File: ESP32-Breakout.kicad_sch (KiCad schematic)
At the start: 3 parts, among them U1 ESP32-S2-DevKitC-1

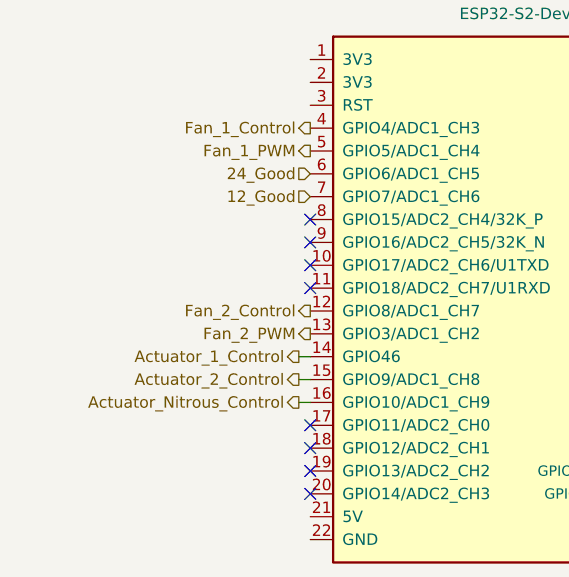
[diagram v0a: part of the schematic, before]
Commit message: Placed the general sets of components.
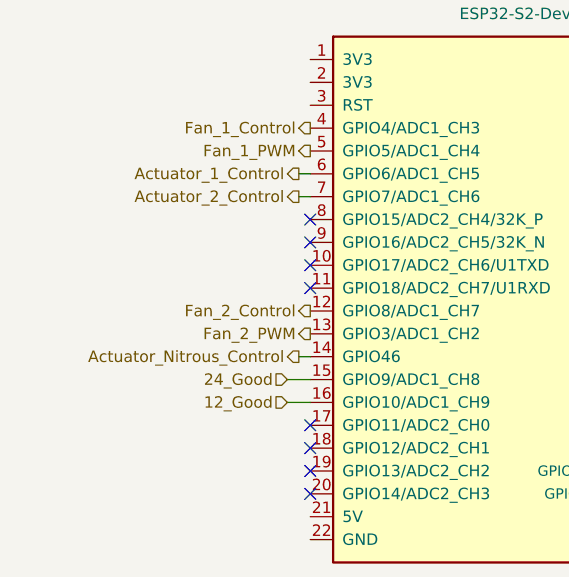
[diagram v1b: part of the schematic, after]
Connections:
- net 12_Good: now also U1.16 (GPIO10/ADC1_CH9); no longer U1.7 (GPIO7/ADC1_CH6)
- net 24_Good: now also U1.15 (GPIO9/ADC1_CH8); no longer U1.6 (GPIO6/ADC1_CH5)
- net Actuator_1_Control: now also U1.6 (GPIO6/ADC1_CH5); no longer U1.14 (GPIO46)
- net Actuator_2_Control: now also U1.7 (GPIO7/ADC1_CH6); no longer U1.15 (GPIO9/ADC1_CH8)
- net Actuator_Nitrous_Control: now also U1.14 (GPIO46); no longer U1.16 (GPIO10/ADC1_CH9)
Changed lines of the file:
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@@
 	(wire
 		(pts
-			(xy 80.01 77.47) (xy 81.28 77.47)
-		)
-		(stroke
-			(width 0)
-			(type default)
-		)
-	)
-	(wire
-		(pts
-			(xy 80.01 74.93) (xy 81.28 74.93)
+			(xy 78.74 77.47) (xy 81.28 77.47)
+		)
+		(stroke
+			(width 0)
+			(type default)
+		)
+	)
+	(wire
+		(pts
+			(xy 78.74 74.93) (xy 81.28 74.93)
 		)
 		(stroke
@@
 		(pts
 			(xy 80.01 72.39) (xy 81.28 72.39)
+		)
+		(stroke
+			(width 0)
+			(type default)
+		)
+	)
+	(wire
+		(pts
+			(xy 80.01 52.07) (xy 81.28 52.07)
+		)
+		(stroke
+			(width 0)
+			(type default)
+		)
+	)
+	(wire
+		(pts
+			(xy 80.01 54.61) (xy 81.28 54.61)
 		)
 		(stroke
@@
 		)
 	)
+	(hierarchical_label "Actuator_Nitrous_Control"
+		(shape output)
+		(at 80.01 72.39 180)
+		(effects
+			(font
+				(size 1.27 1.27)
+			)
+			(justify right)
+		)
+	)
+	(hierarchical_label "Actuator_2_Control"
+		(shape output)
+		(at 80.01 54.61 180)
+		(effects
+			(font
+				(size 1.27 1.27)
+			)
+			(justify right)
+		)
+	)
 	(hierarchical_label "DRDY2"
 		(shape input)
@@
 		)
 	)
-	(hierarchical_label "Actuator_Nitrous_Control"
-		(shape output)
-		(at 80.01 77.47 180)
+	(hierarchical_label "24_Good"
+		(shape input)
+		(at 78.74 74.93 180)
 		(effects
 			(font
@@
 		)
 	)
-	(hierarchical_label "Actuator_2_Control"
-		(shape output)
-		(at 80.01 74.93 180)
+	(hierarchical_label "Actuator_1_Control"
+		(shape output)
+		(at 80.01 52.07 180)
+		(effects
+			(font
+				(size 1.27 1.27)
+			)
+			(justify right)
+		)
+	)
+	(hierarchical_label "12_Good"
+		(shape input)
+		(at 78.74 77.47 180)
 		(effects
 			(font
@@
 		)
 	)
-	(hierarchical_label "24_Good"
-		(shape input)
-		(at 81.28 52.07 180)
-		(effects
-			(font
-				(size 1.27 1.27)
-			)
-			(justify right)
-		)
-	)
-	(hierarchical_label "12_Good"
-		(shape input)
-		(at 81.28 54.61 180)
-		(effects
-			(font
-				(size 1.27 1.27)
-			)
-			(justify right)
-		)
-	)
 	(hierarchical_label "DRDY1"
 		(shape input)
@@
 		(effects
 			(font
-				(size 1.27 1.27)
-			)
-			(justify right)
-		)
-	)
-	(hierarchical_label "Actuator_1_Control"
-		(shape output)
-		(at 80.01 72.39 180)
-		(effects
-			(font

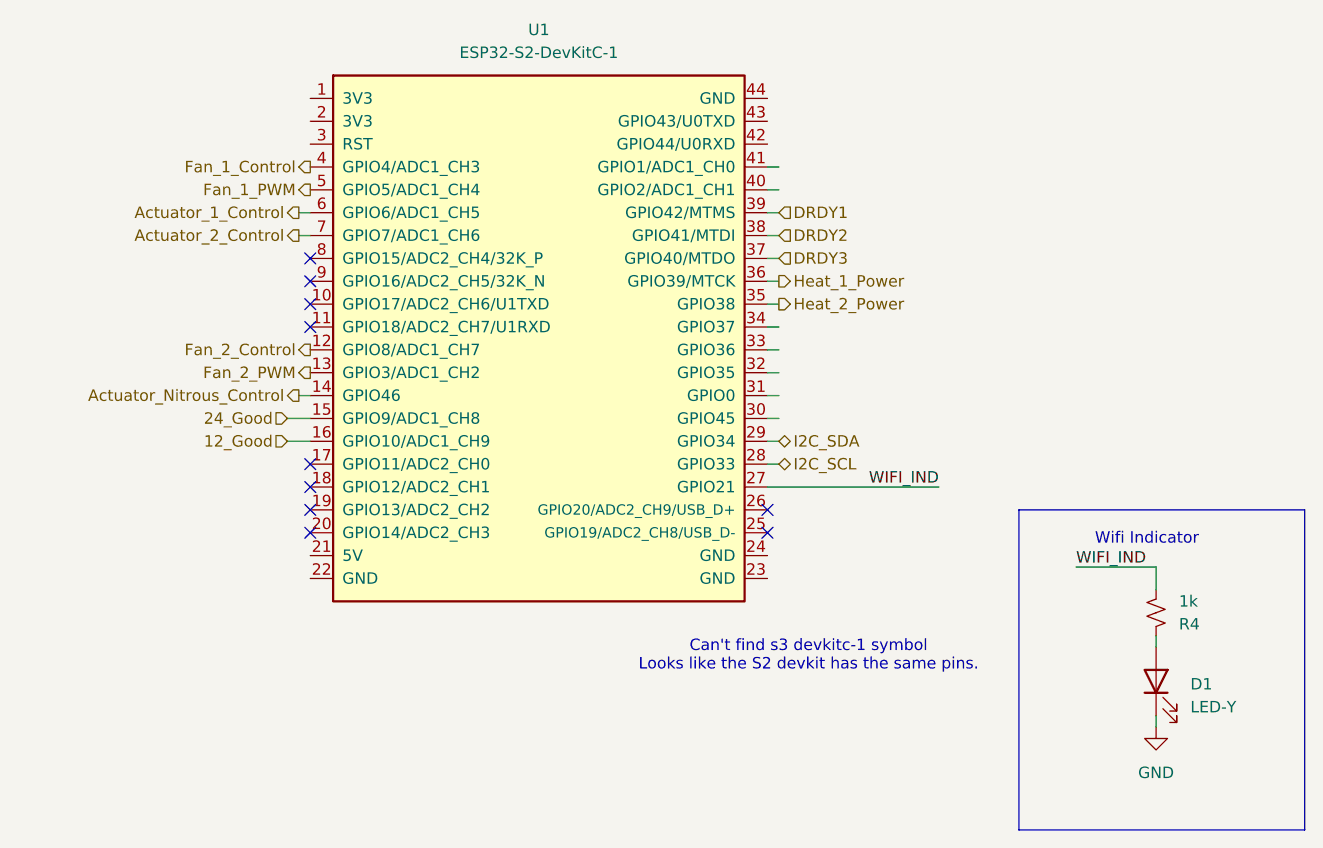
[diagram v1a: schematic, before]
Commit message: General board shape, mounting holes, grounding plates.
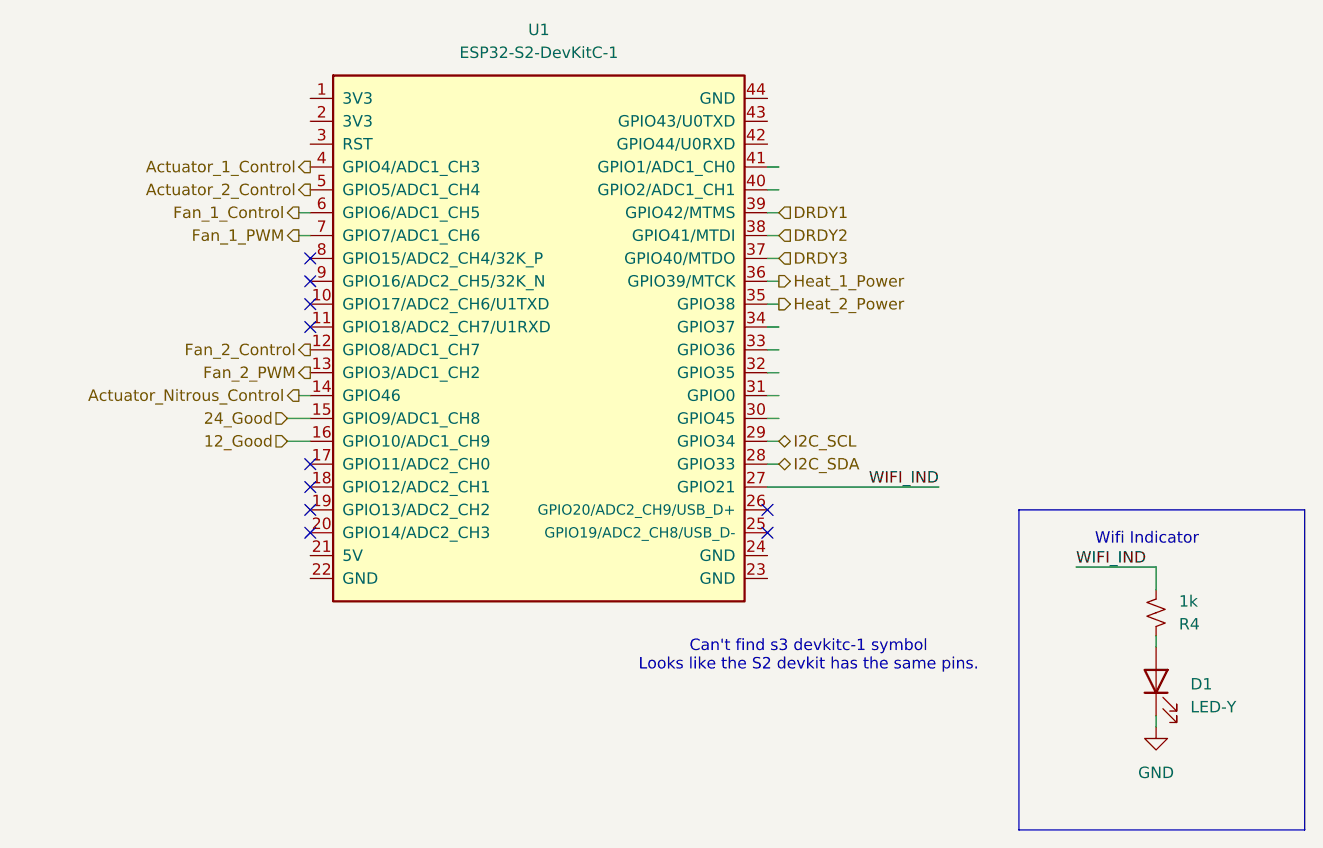
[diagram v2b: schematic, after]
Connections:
- net Actuator_1_Control: now also U1.4 (GPIO4/ADC1_CH3); no longer U1.6 (GPIO6/ADC1_CH5)
- net Actuator_2_Control: now also U1.5 (GPIO5/ADC1_CH4); no longer U1.7 (GPIO7/ADC1_CH6)
- net Fan_1_Control: now also U1.6 (GPIO6/ADC1_CH5); no longer U1.4 (GPIO4/ADC1_CH3)
- net Fan_1_PWM: now also U1.7 (GPIO7/ADC1_CH6); no longer U1.5 (GPIO5/ADC1_CH4)
- net I2C_SCL: now also U1.29 (GPIO34); no longer U1.28 (GPIO33)
- net I2C_SDA: now also U1.28 (GPIO33); no longer U1.29 (GPIO34)
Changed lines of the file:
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@@
 		)
 	)
-	(hierarchical_label "Actuator_Nitrous_Control"
+	(hierarchical_label "Actuator_1_Control"
 		(shape output)
-		(at 80.01 72.39 180)
+		(at 81.28 46.99 180)
 		(effects
 			(font
@@
 		)
 	)
-	(hierarchical_label "Actuator_2_Control"
+	(hierarchical_label "Actuator_Nitrous_Control"
 		(shape output)
-		(at 80.01 54.61 180)
+		(at 80.01 72.39 180)
 		(effects
 			(font
@@
 		)
 	)
-	(hierarchical_label "Fan_1_Control"
-		(shape output)
-		(at 81.28 46.99 180)
-		(effects
-			(font
-				(size 1.27 1.27)
-			)
-			(justify right)
-		)
-	)
-	(hierarchical_label "Actuator_1_Control"
-		(shape output)
-		(at 80.01 52.07 180)
-		(effects
-			(font
-				(size 1.27 1.27)
-			)
-			(justify right)
-		)
-	)
 	(hierarchical_label "12_Good"
 		(shape input)
@@
 		)
 	)
-	(hierarchical_label "I2C_SCL"
-		(shape bidirectional)
-		(at 133.35 80.01 0)
+	(hierarchical_label "Actuator_2_Control"
+		(shape output)
+		(at 81.28 49.53 180)
 		(effects
 			(font
 				(size 1.27 1.27)
 			)
-			(justify left)
+			(justify right)
 		)
 	)
@@
 		)
 	)
-	(hierarchical_label "Fan_1_PWM"
-		(shape output)
-		(at 81.28 49.53 180)
-		(effects
-			(font
-				(size 1.27 1.27)
-			)
-			(justify right)
-		)
-	)
 	(hierarchical_label "Fan_2_Control"
 		(shape output)
@@
 		)
 	)
+	(hierarchical_label "Fan_1_Control"
+		(shape output)
+		(at 80.01 52.07 180)
+		(effects
+			(font
+				(size 1.27 1.27)
+			)
+			(justify right)
+		)
+	)
+	(hierarchical_label "I2C_SCL"
+		(shape bidirectional)
+		(at 133.35 77.47 0)
+		(effects
+			(font
+				(size 1.27 1.27)
+			)
+			(justify left)
+		)
+	)
 	(hierarchical_label "I2C_SDA"
 		(shape bidirectional)
-		(at 133.35 77.47 0)
+		(at 133.35 80.01 0)
 		(effects
 			(font
@@
 		)
 	)
+	(hierarchical_label "Fan_1_PWM"
+		(shape output)
+		(at 80.01 54.61 180)
+		(effects
+			(font
+				(size 1.27 1.27)
+			)
+			(justify right)
+		)
+	)

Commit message: Second draft of placement and wiring.
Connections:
- net DRDY1: now also U1.34 (GPIO37); no longer U1.39 (GPIO42/MTMS)
- net DRDY2: now also U1.39 (GPIO42/MTMS); no longer U1.38 (GPIO41/MTDI)
- net DRDY3: now also U1.30 (GPIO45); no longer U1.37 (GPIO40/MTDO)
- net WIFI_IND: now also U1.43 (GPIO43/U0TXD); no longer U1.27 (GPIO21)
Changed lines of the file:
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@@
+	(wire
+		(pts
+			(xy 132.08 41.91) (xy 140.97 41.91)
+		)
+		(stroke
+			(width 0)
+			(type default)
+		)
+	)
 	(wire
 		(pts
@@
 			(width 0)
 			(type default)
-		)
-	)
-	(label "WIFI_IND"
-		(at 151.13 82.55 180)
-		(effects
-			(font
-				(size 1.27 1.27)
-			)
-			(justify right bottom)
 		)
 	)
@@
 		)
 	)
+	(label "WIFI_IND"
+		(at 140.97 41.91 0)
+		(effects
+			(font
+				(size 1.27 1.27)
+			)
+			(justify left bottom)
+		)
+	)
 	(hierarchical_label "Actuator_1_Control"
 		(shape output)
@@
 		)
 	)
+	(hierarchical_label "DRDY3"
+		(shape input)
+		(at 133.35 74.93 0)
+		(effects
+			(font
+				(size 1.27 1.27)
+			)
+			(justify left)
+		)
+	)
+	(hierarchical_label "Heat_1_Power"
+		(shape output)
+		(at 133.35 59.69 0)
+		(effects
+			(font
+				(size 1.27 1.27)
+			)
+			(justify left)
+		)
+	)
+	(hierarchical_label "24_Good"
+		(shape input)
+		(at 78.74 74.93 180)
+		(effects
+			(font
+				(size 1.27 1.27)
+			)
+			(justify right)
+		)
+	)
+	(hierarchical_label "Heat_2_Power"
+		(shape output)
+		(at 133.35 62.23 0)
+		(effects
+			(font
+				(size 1.27 1.27)
+			)
+			(justify left)
+		)
+	)
+	(hierarchical_label "12_Good"
+		(shape input)
+		(at 78.74 77.47 180)
+		(effects
+			(font
+				(size 1.27 1.27)
+			)
+			(justify right)
+		)
+	)
 	(hierarchical_label "DRDY2"
 		(shape input)
-		(at 133.35 54.61 0)
-		(effects
-			(font
-				(size 1.27 1.27)
-			)
-			(justify left)
-		)
-	)
-	(hierarchical_label "Heat_1_Power"
-		(shape output)
-		(at 133.35 59.69 0)
-		(effects
-			(font
-				(size 1.27 1.27)
-			)
-			(justify left)
-		)
-	)
-	(hierarchical_label "24_Good"
-		(shape input)
-		(at 78.74 74.93 180)
-		(effects
-			(font
-				(size 1.27 1.27)
-			)
-			(justify right)
-		)
-	)
-	(hierarchical_label "Heat_2_Power"
-		(shape output)
-		(at 133.35 62.23 0)
-		(effects
-			(font
-				(size 1.27 1.27)
-			)
-			(justify left)
-		)
-	)
-	(hierarchical_label "12_Good"
-		(shape input)
-		(at 78.74 77.47 180)
-		(effects
-			(font
-				(size 1.27 1.27)
-			)
-			(justify right)
+		(at 133.35 52.07 0)
+		(effects
+			(font
+				(size 1.27 1.27)
+			)
+			(justify left)
 		)
 	)
@@
 			)
 			(justify right)
-		)
-	)
-	(hierarchical_label "DRDY1"
-		(shape input)
-		(at 133.35 52.07 0)
-		(effects
-			(font
-				(size 1.27 1.27)
-			)
-			(justify left)
 		)
 	)
@@
 		)
 	)
+	(hierarchical_label "DRDY1"
+		(shape input)
+		(at 133.35 64.77 0)
+		(effects
+			(font
+				(size 1.27 1.27)
+			)
+			(justify left)
+		)
+	)
 	(hierarchical_label "I2C_SDA"
 		(shape bidirectional)
@@
 		)
 	)
-	(hierarchical_label "DRDY3"
-		(shape input)
-		(at 133.35 57.15 0)
-		(effects
-			(font
-				(size 1.27 1.27)
-			)
-			(justify left)
-		)
-	)
